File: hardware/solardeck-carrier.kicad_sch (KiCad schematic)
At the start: 0 parts

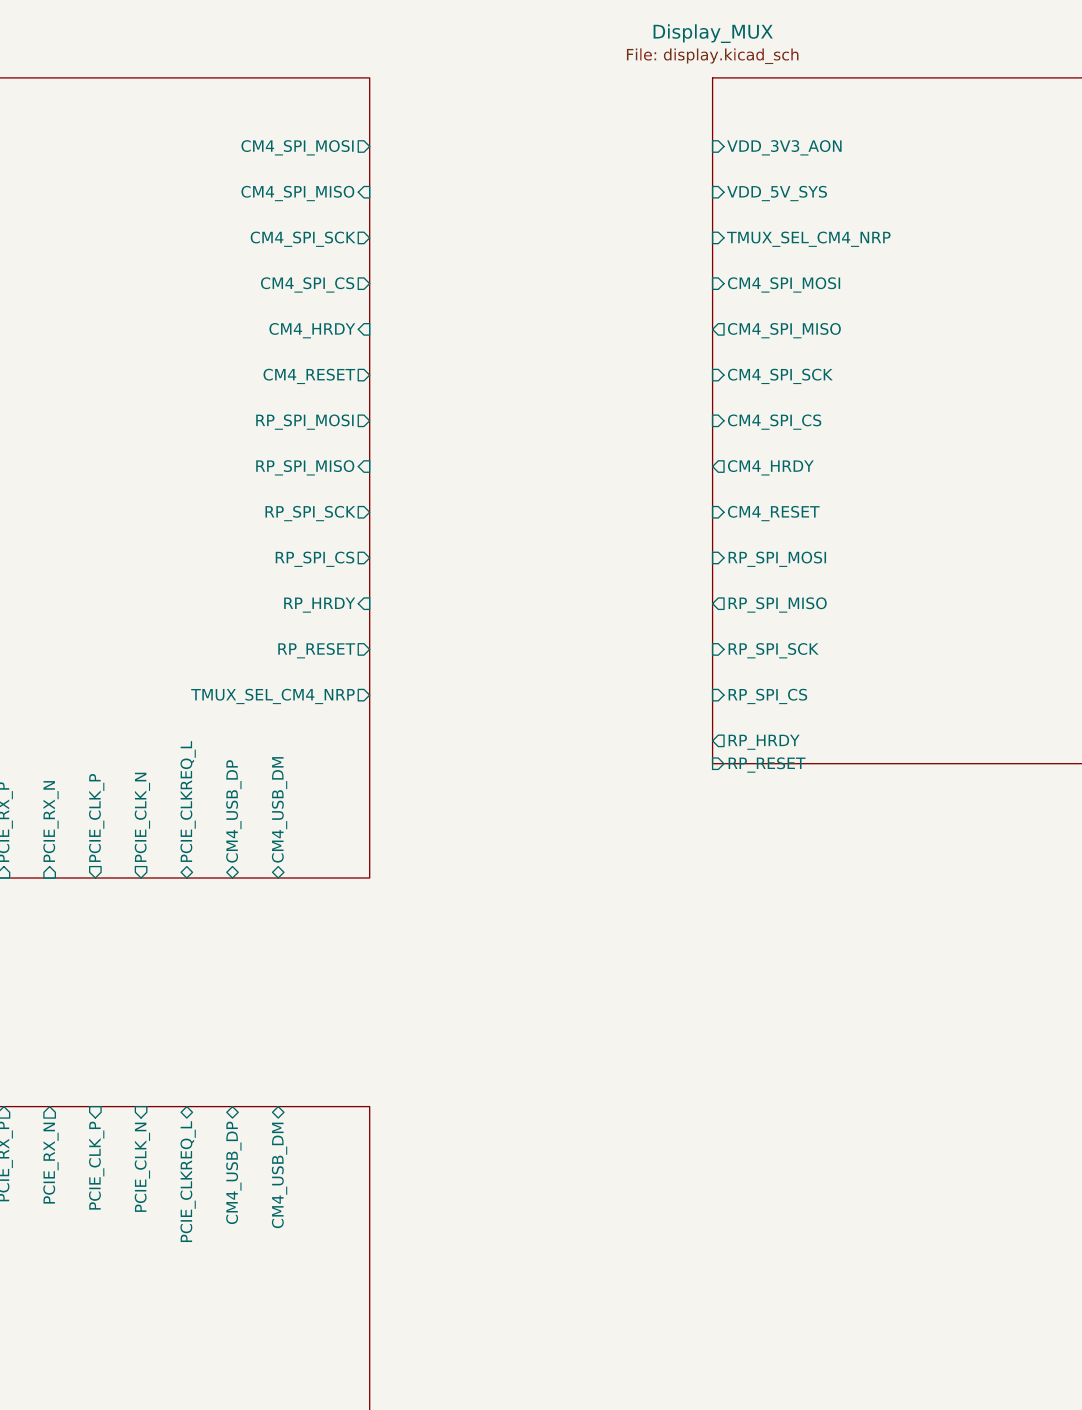
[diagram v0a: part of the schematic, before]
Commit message: AUDIT 6 + README rewrite; standardize on CM5, Kaleido 4, SGP.22 eSIM
Class: C1 CLAIM + C4 HYGIENE (spans C2 for the overlay/identifier rename).

- docs/AUDIT_6_2026-10-21.md: repo checked against datasheets. Blockers: BQ25895
  cannot charge LiFePO4 (VREG floor 3.84 V, default 4.208 V); protector and gauge are
  Li-ion parts; CM4/CM5 have no RAM-retaining low-power state; panel/stack/cell do
  not close; schematic has no connectivity; ~half the LCSC numbers are wrong.
- README.md rewritten: intent first, pillars with real status, one status section.
- ADR-031 CM5116064 is the compute standard; ADR-032 Kaleido 4 is the only panel,
  V1 waits for release (supersedes ADR-030 two-SKU); ADR-033 soldered eSIM kept,
  must be consumer SGP.22 (ST4SIM-200M rejected).
- spec_values: panel facts, reader geometry, refresh timings, epdc_spi_mhz -> null;
  CM5 supply keys; BCM2712 (was BCM2718); BOM total re-derived as a floor.
- Gates: two dead BANNED regexes fixed (red-controlled); Phase 9 accepts any
  harness attribution and no longer claims link checking; Phases 5/10 skip null
  panel facts with an UNVERIFIED line; Phase 14 counts TBD rows; Phase 16 checks
  the CM5 commitment is stated as unpublished.
- Sweep: CM4 -> CM5 across live docs, firmware identifiers, nets, production
  guides; overlay renamed solardeck-cm5.dts and marked not yet valid (RP1 port).
- Airgap switch: ties CM5 WL_nDisable/BT_nDisable low (CM5 datasheet 2.1.1-2.1.2).

verify_all.py: 16/16 green. Still unmeasured: everything.

Co-Authored-By: Claude Opus 5.5 <noreply@anthropic.com>
Harness: claude-code (anthropic/claude-opus-5-5, session f5d955c0)
Claude-Session: https://claude.ai/code/session_01CkqVCXjctA16Vs1i2pskTP
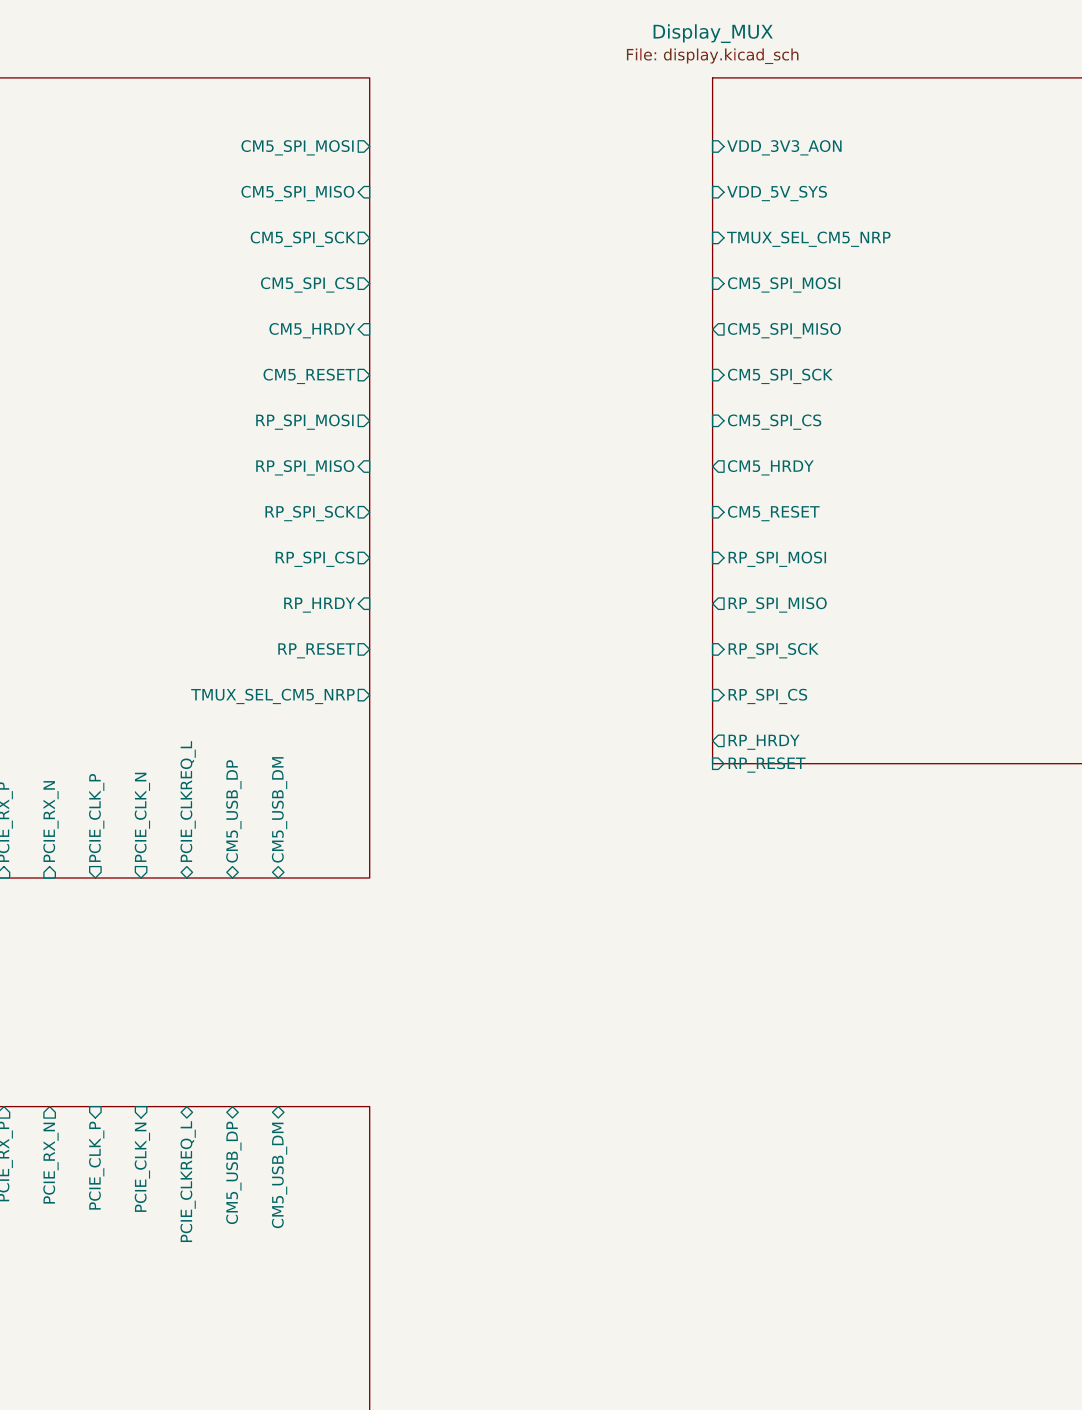
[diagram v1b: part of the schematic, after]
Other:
- sheet Compute_DualBrain ports: added CM5_HRDY, CM5_RESET, CM5_SPI_CS, CM5_SPI_MISO, CM5_SPI_MOSI, CM5_SPI_SCK, CM5_USB_DM, CM5_USB_DP, TMUX_SEL_CM5_NRP; removed CM4_HRDY, CM4_RESET, CM4_SPI_CS, CM4_SPI_MISO, CM4_SPI_MOSI, CM4_SPI_SCK, CM4_USB_DM, CM4_USB_DP, TMUX_SEL_CM4_NRP
- sheet Display_MUX ports: added CM5_HRDY, CM5_RESET, CM5_SPI_CS, CM5_SPI_MISO, CM5_SPI_MOSI, CM5_SPI_SCK, TMUX_SEL_CM5_NRP; removed CM4_HRDY, CM4_RESET, CM4_SPI_CS, CM4_SPI_MISO, CM4_SPI_MOSI, CM4_SPI_SCK, TMUX_SEL_CM4_NRP
- sheet IO_Peripherals ports: added CM5_USB_DM, CM5_USB_DP; removed CM4_USB_DM, CM4_USB_DP
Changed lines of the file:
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@@
   )
   ;; =========================================================================
-  ;; SHEET 2: Dual-Brain Compute (CM4 + RP2350B)
+  ;; SHEET 2: Dual-Brain Compute (CM5 + RP2350B)
   ;; =========================================================================
   (sheet (at 127.0 38.1) (size 101.6 88.9)
@@
     (pin "SOLAR_ADC_IN" input (at 127.0 71.12 180))
     (pin "CHEM_SEL_RP" input (at 127.0 76.2 180))
-    ;; Display SPI CM4 & RP
-    (pin "CM4_SPI_MOSI" output (at 228.6 45.72 0))
-    (pin "CM4_SPI_MISO" input (at 228.6 50.8 0))
-    (pin "CM4_SPI_SCK" output (at 228.6 55.88 0))
-    (pin "CM4_SPI_CS" output (at 228.6 60.96 0))
-    (pin "CM4_HRDY" input (at 228.6 66.04 0))
-    (pin "CM4_RESET" output (at 228.6 71.12 0))
+    ;; Display SPI CM5 & RP
+    (pin "CM5_SPI_MOSI" output (at 228.6 45.72 0))
+    (pin "CM5_SPI_MISO" input (at 228.6 50.8 0))
+    (pin "CM5_SPI_SCK" output (at 228.6 55.88 0))
+    (pin "CM5_SPI_CS" output (at 228.6 60.96 0))
+    (pin "CM5_HRDY" input (at 228.6 66.04 0))
+    (pin "CM5_RESET" output (at 228.6 71.12 0))
     (pin "RP_SPI_MOSI" output (at 228.6 76.2 0))
     (pin "RP_SPI_MISO" input (at 228.6 81.28 0))
@@
     (pin "RP_HRDY" input (at 228.6 96.52 0))
     (pin "RP_RESET" output (at 228.6 101.6 0))
-    (pin "TMUX_SEL_CM4_NRP" output (at 228.6 106.68 0))
+    (pin "TMUX_SEL_CM5_NRP" output (at 228.6 106.68 0))
     ;; PCIe & USB to I/O
     (pin "PCIE_TX_P" output (at 177.8 127.0 270))
@@
     (pin "PCIE_CLK_N" output (at 203.2 127.0 270))
     (pin "PCIE_CLKREQ_L" bidirectional (at 208.28 127.0 270))
-    (pin "CM4_USB_DP" bidirectional (at 213.36 127.0 270))
-    (pin "CM4_USB_DM" bidirectional (at 218.44 127.0 270))
+    (pin "CM5_USB_DP" bidirectional (at 213.36 127.0 270))
+    (pin "CM5_USB_DM" bidirectional (at 218.44 127.0 270))
   )
   ;; =========================================================================
@@
     (pin "VDD_3V3_AON" input (at 266.7 45.72 180))
     (pin "VDD_5V_SYS" input (at 266.7 50.8 180))
-    (pin "TMUX_SEL_CM4_NRP" input (at 266.7 55.88 180))
-    (pin "CM4_SPI_MOSI" input (at 266.7 60.96 180))
-    (pin "CM4_SPI_MISO" output (at 266.7 66.04 180))
-    (pin "CM4_SPI_SCK" input (at 266.7 71.12 180))
-    (pin "CM4_SPI_CS" input (at 266.7 76.2 180))
-    (pin "CM4_HRDY" output (at 266.7 81.28 180))
-    (pin "CM4_RESET" input (at 266.7 86.36 180))
+    (pin "TMUX_SEL_CM5_NRP" input (at 266.7 55.88 180))
+    (pin "CM5_SPI_MOSI" input (at 266.7 60.96 180))
+    (pin "CM5_SPI_MISO" output (at 266.7 66.04 180))
+    (pin "CM5_SPI_SCK" input (at 266.7 71.12 180))
+    (pin "CM5_SPI_CS" input (at 266.7 76.2 180))
+    (pin "CM5_HRDY" output (at 266.7 81.28 180))
+    (pin "CM5_RESET" input (at 266.7 86.36 180))
     (pin "RP_SPI_MOSI" input (at 266.7 91.44 180))
     (pin "RP_SPI_MISO" output (at 266.7 96.52 180))
@@
     (pin "PCIE_CLK_N" input (at 203.2 152.4 90))
     (pin "PCIE_CLKREQ_L" bidirectional (at 208.28 152.4 90))
-    (pin "CM4_USB_DP" bidirectional (at 213.36 152.4 90))
-    (pin "CM4_USB_DM" bidirectional (at 218.44 152.4 90))
+    (pin "CM5_USB_DP" bidirectional (at 213.36 152.4 90))
+    (pin "CM5_USB_DM" bidirectional (at 218.44 152.4 90))
   )
 )
